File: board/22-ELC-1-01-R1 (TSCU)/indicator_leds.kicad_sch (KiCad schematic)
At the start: 8 parts

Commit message: More work
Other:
- moved on the sheet: D?, R?, U?A
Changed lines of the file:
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@@
   (junction (at 83.82 85.09) (diameter 0) (color 0 0 0 0)
   )
-  (junction (at 85.09 120.65) (diameter 0) (color 0 0 0 0)
-  )
-  (wire (pts (xy 60.96 132.08) (xy 60.96 123.19))
-    (stroke (width 0) (type default) (color 0 0 0 0))
-  )
-  (wire (pts (xy 111.76 120.65) (xy 115.57 120.65))
-    (stroke (width 0) (type default) (color 0 0 0 0))
-  )
-  (wire (pts (xy 85.09 120.65) (xy 85.09 132.08))
+  (junction (at 83.82 120.65) (diameter 0) (color 0 0 0 0)
+  )
+  (wire (pts (xy 59.69 132.08) (xy 59.69 123.19))
+    (stroke (width 0) (type default) (color 0 0 0 0))
+  )
+  (wire (pts (xy 110.49 120.65) (xy 114.3 120.65))
+    (stroke (width 0) (type default) (color 0 0 0 0))
+  )
+  (wire (pts (xy 83.82 120.65) (xy 83.82 132.08))
     (stroke (width 0) (type default) (color 0 0 0 0))
   )
@@
     (stroke (width 0) (type default) (color 0 0 0 0))
   )
-  (wire (pts (xy 90.17 120.65) (xy 85.09 120.65))
-    (stroke (width 0) (type default) (color 0 0 0 0))
-  )
-  (wire (pts (xy 80.01 120.65) (xy 85.09 120.65))
+  (wire (pts (xy 88.9 120.65) (xy 83.82 120.65))
+    (stroke (width 0) (type default) (color 0 0 0 0))
+  )
+  (wire (pts (xy 78.74 120.65) (xy 83.82 120.65))
     (stroke (width 0) (type default) (color 0 0 0 0))
   )
@@
     (stroke (width 0) (type default) (color 0 0 0 0))
   )
-  (wire (pts (xy 115.57 120.65) (xy 115.57 123.19))
+  (wire (pts (xy 114.3 120.65) (xy 114.3 123.19))
     (stroke (width 0) (type default) (color 0 0 0 0))
   )
@@
     (stroke (width 0) (type default) (color 0 0 0 0))
   )
-  (wire (pts (xy 85.09 132.08) (xy 60.96 132.08))
+  (wire (pts (xy 83.82 132.08) (xy 59.69 132.08))
     (stroke (width 0) (type default) (color 0 0 0 0))
   )
@@
     (stroke (width 0) (type default) (color 0 0 0 0))
   )
-  (wire (pts (xy 97.79 120.65) (xy 104.14 120.65))
-    (stroke (width 0) (type default) (color 0 0 0 0))
-  )
-  (wire (pts (xy 46.99 118.11) (xy 64.77 118.11))
-    (stroke (width 0) (type default) (color 0 0 0 0))
-  )
-  (wire (pts (xy 60.96 123.19) (xy 64.77 123.19))
+  (wire (pts (xy 96.52 120.65) (xy 102.87 120.65))
+    (stroke (width 0) (type default) (color 0 0 0 0))
+  )
+  (wire (pts (xy 46.99 118.11) (xy 63.5 118.11))
+    (stroke (width 0) (type default) (color 0 0 0 0))
+  )
+  (wire (pts (xy 59.69 123.19) (xy 63.5 123.19))
     (stroke (width 0) (type default) (color 0 0 0 0))
   )
@@
     (pin "8")
   )
-  (symbol (lib_id "power:GND") (at 115.57 123.19 0) (unit 1)
-    (in_bom yes) (on_board yes) (fields_autoplaced)
-    (property "Reference" "#PWR?" (id 0) (at 115.57 129.54 0)
-      (effects (font (size 1.27 1.27)) hide)
-    )
-    (property "Value" "GND" (id 1) (at 115.57 128.27 0))
-    (property "Footprint" "" (id 2) (at 115.57 123.19 0)
-      (effects (font (size 1.27 1.27)) hide)
-    )
-    (property "Datasheet" "" (id 3) (at 115.57 123.19 0)
-      (effects (font (size 1.27 1.27)) hide)
-    )
-    (pin "1")
-  )
-  (symbol (lib_id "Amplifier_Operational:LM358") (at 72.39 120.65 0) (unit 1)
-    (in_bom yes) (on_board yes) (fields_autoplaced)
-    (property "Reference" "U?" (id 0) (at 72.39 110.49 0))
-    (property "Value" "LM358" (id 1) (at 72.39 113.03 0))
-    (property "Footprint" "" (id 2) (at 72.39 120.65 0)
-      (effects (font (size 1.27 1.27)) hide)
-    )
-    (property "Datasheet" "http://www.ti.com/lit/ds/symlink/lm2904-n.pdf" (id 3) (at 72.39 120.65 0)
+  (symbol (lib_id "power:GND") (at 114.3 123.19 0) (unit 1)
+    (in_bom yes) (on_board yes) (fields_autoplaced)
+    (property "Reference" "#PWR?" (id 0) (at 114.3 129.54 0)
+      (effects (font (size 1.27 1.27)) hide)
+    )
+    (property "Value" "GND" (id 1) (at 114.3 128.27 0))
+    (property "Footprint" "" (id 2) (at 114.3 123.19 0)
+      (effects (font (size 1.27 1.27)) hide)
+    )
+    (property "Datasheet" "" (id 3) (at 114.3 123.19 0)
+      (effects (font (size 1.27 1.27)) hide)
+    )
+    (pin "1")
+  )
+  (symbol (lib_id "Amplifier_Operational:LM358") (at 71.12 120.65 0) (unit 1)
+    (in_bom yes) (on_board yes) (fields_autoplaced)
+    (property "Reference" "U?" (id 0) (at 71.12 110.49 0))
+    (property "Value" "LM358" (id 1) (at 71.12 113.03 0))
+    (property "Footprint" "" (id 2) (at 71.12 120.65 0)
+      (effects (font (size 1.27 1.27)) hide)
+    )
+    (property "Datasheet" "http://www.ti.com/lit/ds/symlink/lm2904-n.pdf" (id 3) (at 71.12 120.65 0)
       (effects (font (size 1.27 1.27)) hide)
     )
@@
     (pin "8")
   )
-  (symbol (lib_id "Device:R") (at 93.98 120.65 90) (unit 1)
-    (in_bom yes) (on_board yes) (fields_autoplaced)
-    (property "Reference" "R?" (id 0) (at 93.98 114.3 90))
-    (property "Value" "220" (id 1) (at 93.98 116.84 90))
-    (property "Footprint" "" (id 2) (at 93.98 122.428 90)
-      (effects (font (size 1.27 1.27)) hide)
-    )
-    (property "Datasheet" "~" (id 3) (at 93.98 120.65 0)
-      (effects (font (size 1.27 1.27)) hide)
-    )
-    (pin "1")
-    (pin "2")
-  )
-  (symbol (lib_id "Device:LED") (at 107.95 120.65 180) (unit 1)
-    (in_bom yes) (on_board yes) (fields_autoplaced)
-    (property "Reference" "D?" (id 0) (at 109.5375 113.03 0))
-    (property "Value" "IMS_FAULT_LED" (id 1) (at 109.5375 115.57 0))
-    (property "Footprint" "" (id 2) (at 107.95 120.65 0)
-      (effects (font (size 1.27 1.27)) hide)
-    )
-    (property "Datasheet" "~" (id 3) (at 107.95 120.65 0)
-      (effects (font (size 1.27 1.27)) hide)
-    )
+  (symbol (lib_id "Device:R") (at 92.71 120.65 90) (unit 1)
+    (in_bom yes) (on_board yes) (fields_autoplaced)
+    (property "Reference" "R?" (id 0) (at 92.71 114.3 90))
+    (property "Value" "220" (id 1) (at 92.71 116.84 90))
+    (property "Footprint" "" (id 2) (at 92.71 122.428 90)
+      (effects (font (size 1.27 1.27)) hide)
+    )
+    (property "Datasheet" "~" (id 3) (at 92.71 120.65 0)
+      (effects (font (size 1.27 1.27)) hide)
+    )
+    (pin "1")
+    (pin "2")
+  )
+  (symbol (lib_id "Device:LED") (at 106.68 120.65 180) (unit 1)
+    (in_bom yes) (on_board yes) (fields_autoplaced)
+    (property "Reference" "D?" (id 0) (at 108.2675 113.03 0))
+    (property "Value" "IMS_FAULT_LED" (id 1) (at 108.2675 115.57 0))
+    (property "Footprint" "" (id 2) (at 106.68 120.65 0)
+      (effects (font (size 1.27 1.27)) hide)
+    )
+    (property "Datasheet" "~" (id 3) (at 106.68 120.65 0)
+      (effects (font (size 1.27 1.27)) hide)
+    )

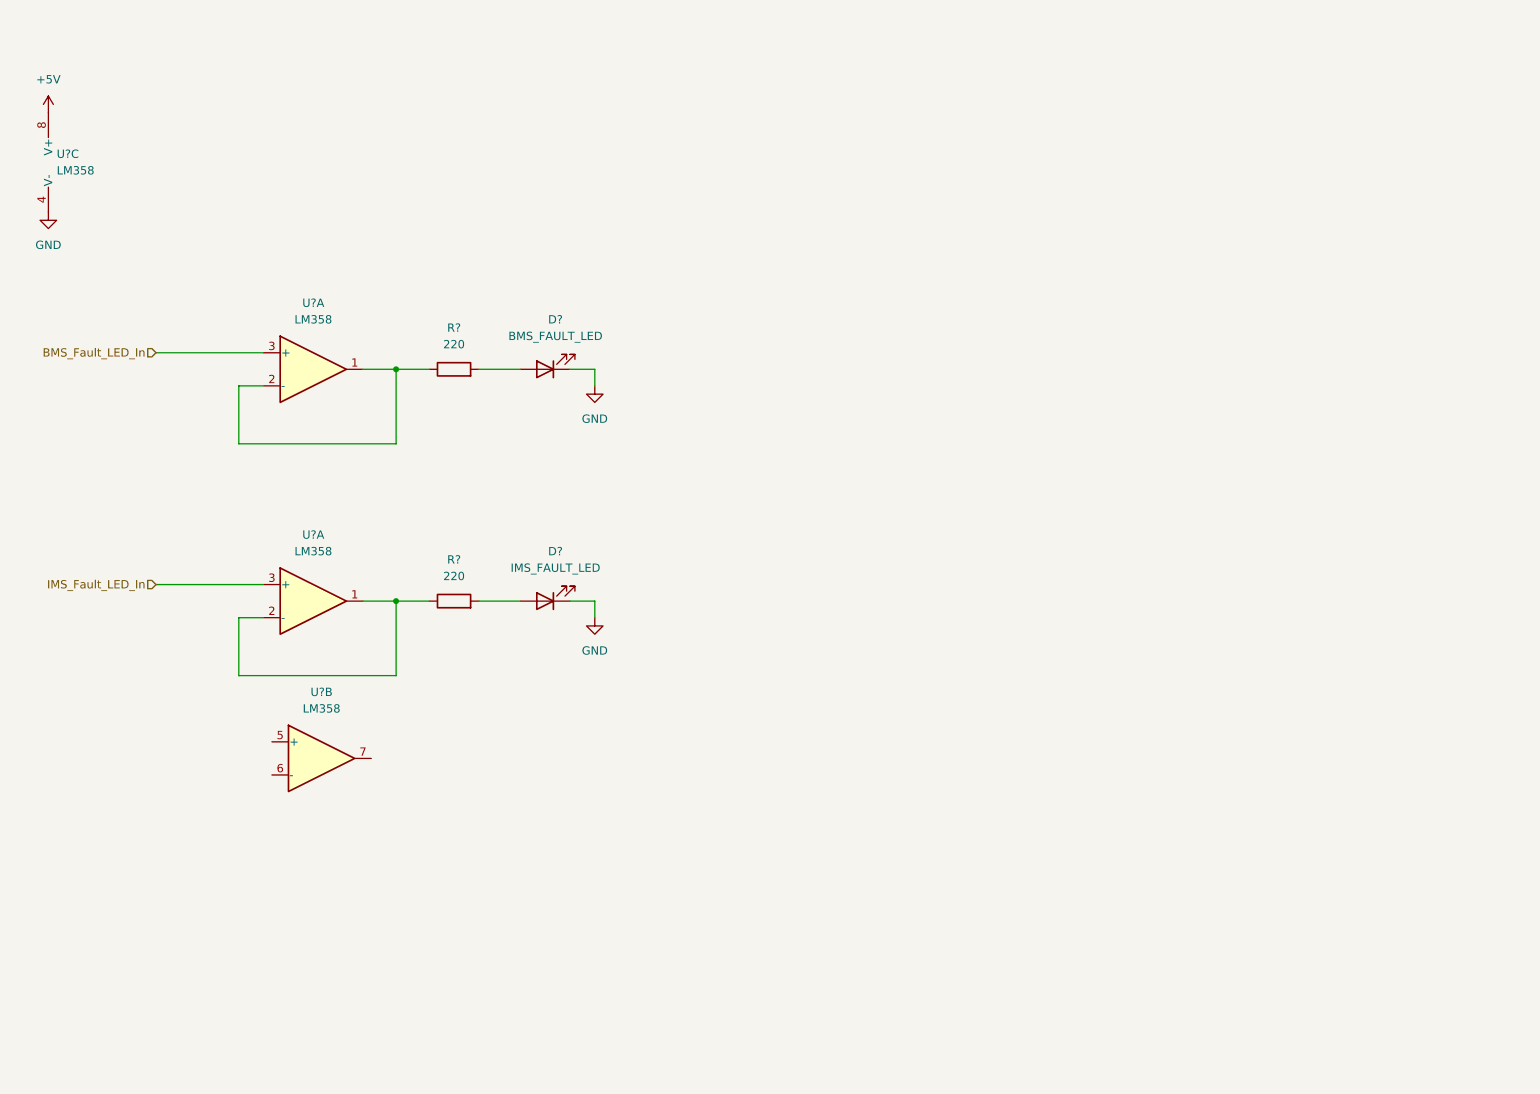
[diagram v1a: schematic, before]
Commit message: More LEDs and test points
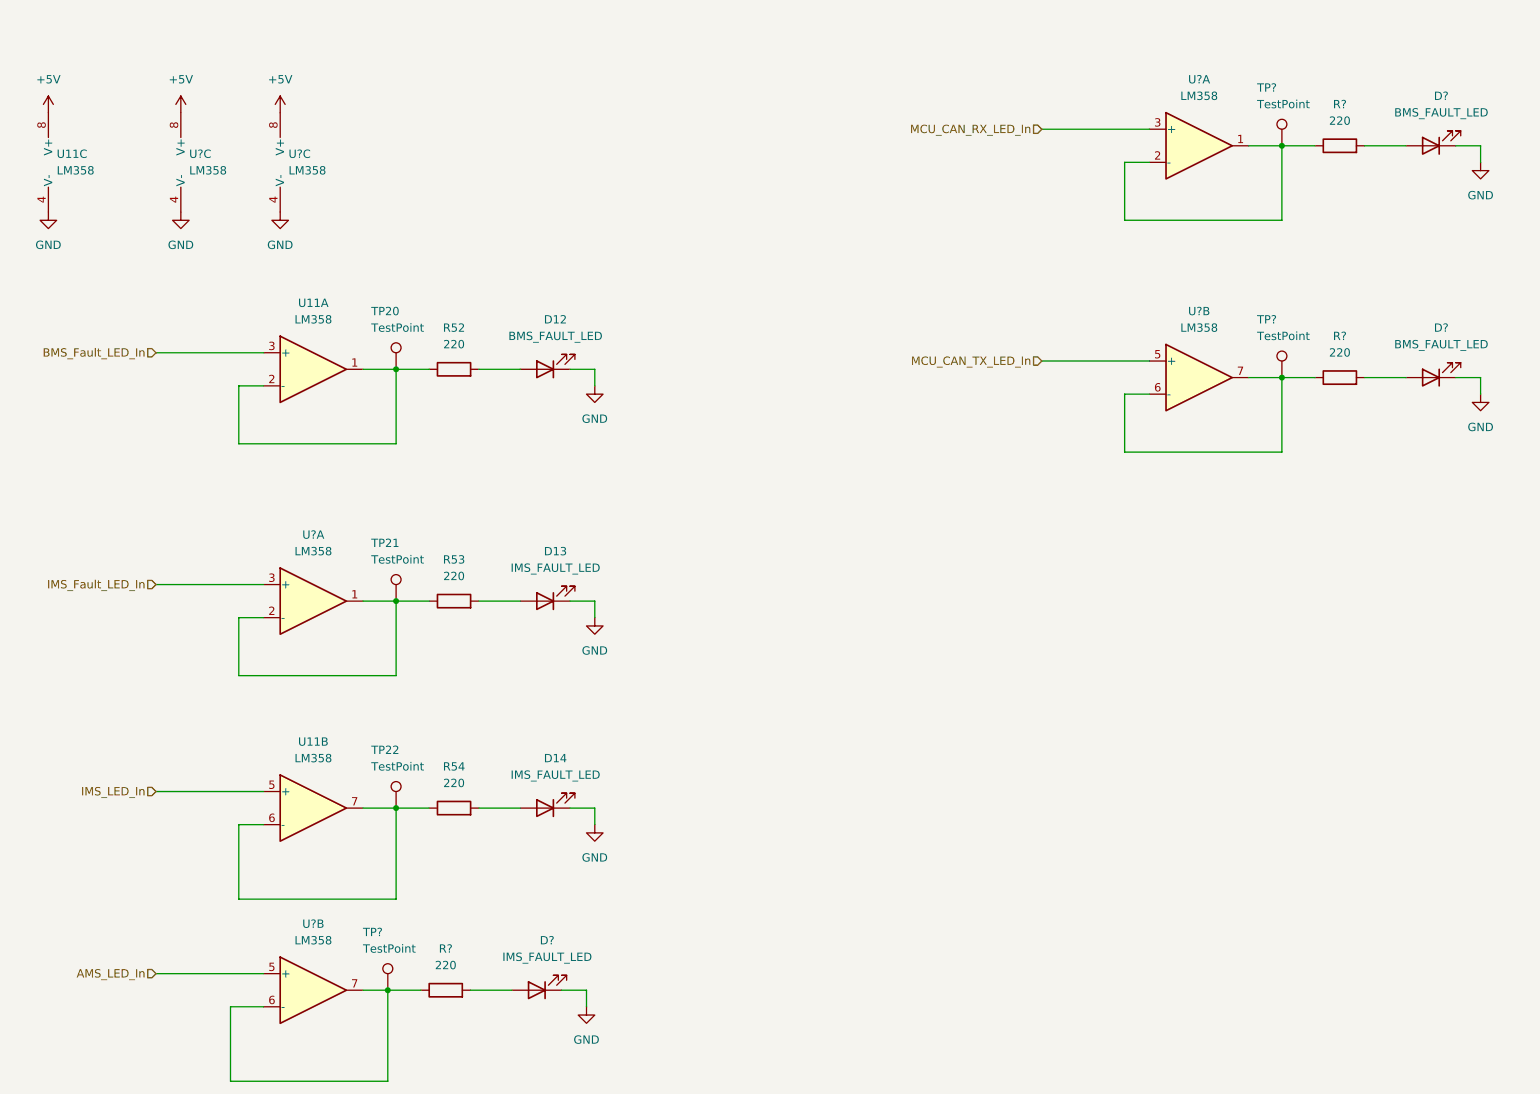
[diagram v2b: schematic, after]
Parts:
- removed U?: LM358, symbol Amplifier_Operational:LM358
- added D14, D?: IMS_FAULT_LED, symbol Device:LED
- added D? (x2): BMS_FAULT_LED, symbol Device:LED
- added R54, R? (x3): 220, symbol Device:R
- added TP20, TP21, TP22, TP? (x3): TestPoint, symbol Connector:TestPoint
- added U? (x6): LM358, symbol Amplifier_Operational:LM358
- gave numbers to parts that had none: 5
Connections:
- net +5V: now also U?.8 (V+), U?.8 (V+)
- net GND: now also D14.1 (K), D?.1 (K), D?.1 (K), D?.1 (K), U?.4 (V-), U?.4 (V-)
- net IMS_Fault_LED_In: now also U?.3 (+)
- net IMS_LED_In: now reaches U11.5 (+)
- net at U11.6 (-): now also U11.7, R54.1, TP22.1
- net at R53.1: now also TP21.1, U?.1, U?.2 (-)
- net at R52.1, U11.1, U11.2 (-): now also TP20.1
- new net: R?.1, TP?.1, U?.6 (-), U?.7 (x2)
- new net: D14.2 (A), R54.2
- new net: R?.1, TP?.1, U?.1, U?.2 (-)
- new net: D?.2 (A), R?.2 (x3)
- new net AMS_LED_In: U?.5 (+)
- new net MCU_CAN_RX_LED_In: U?.3 (+)
- new net MCU_CAN_TX_LED_In: U?.5 (+)
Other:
- moved on the sheet: U11B

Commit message: More LEDs and TPs
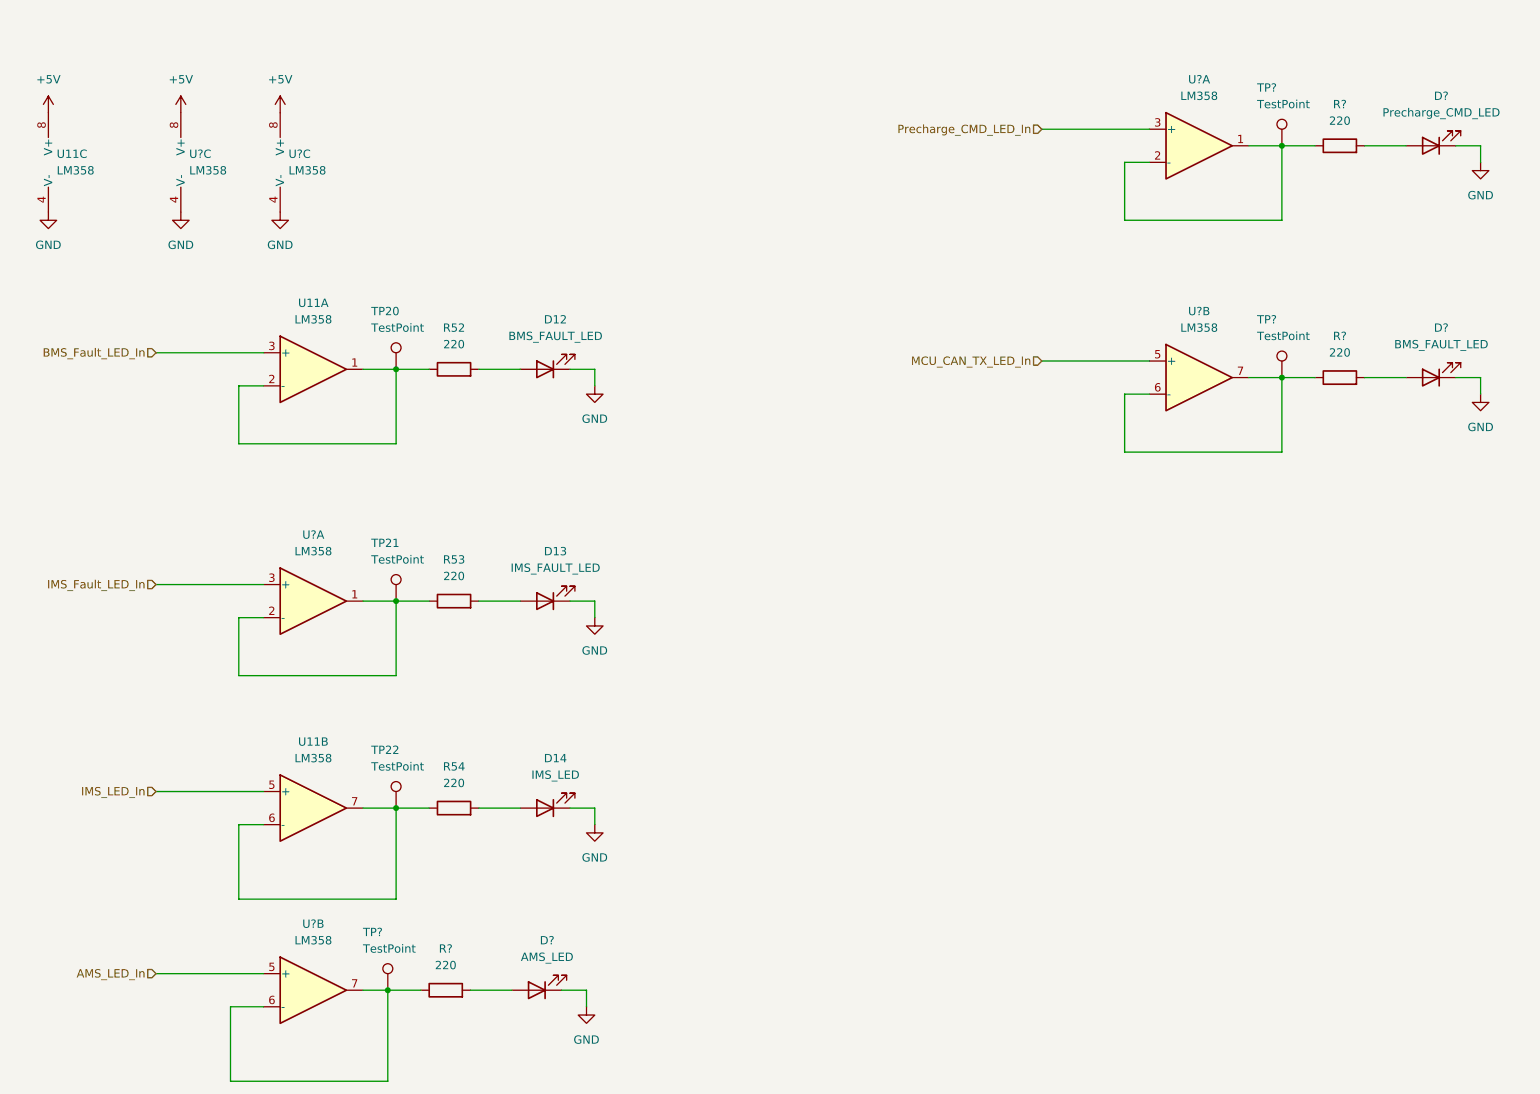
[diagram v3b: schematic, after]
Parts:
- D14: value IMS_FAULT_LED -> IMS_LED
- D?: value BMS_FAULT_LED -> Precharge_CMD_LED
- D?: value IMS_FAULT_LED -> AMS_LED
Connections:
- net MCU_CAN_RX_LED_In renamed Precharge_CMD_LED_In
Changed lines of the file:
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@@
     (effects (font (size 1.27 1.27)) (justify right))
   )
-  (hierarchical_label "MCU_CAN_RX_LED_In" (shape input) (at 182.88 48.26 180)
+  (hierarchical_label "Precharge_CMD_LED_In" (shape input) (at 182.88 48.26 180)
     (effects (font (size 1.27 1.27)) (justify right))
   )
@@
     (in_bom yes) (on_board yes) (fields_autoplaced)
     (property "Reference" "D?" (id 0) (at 244.1575 43.18 0))
-    (property "Value" "BMS_FAULT_LED" (id 1) (at 244.1575 45.72 0))
+    (property "Value" "Precharge_CMD_LED" (id 1) (at 244.1575 45.72 0))
     (property "Footprint" "" (id 2) (at 242.57 50.8 0)
       (effects (font (size 1.27 1.27)) hide)
@@
     (in_bom yes) (on_board yes) (fields_autoplaced)
     (property "Reference" "D14" (id 0) (at 108.2675 144.78 0))
-    (property "Value" "IMS_FAULT_LED" (id 1) (at 108.2675 147.32 0))
+    (property "Value" "IMS_LED" (id 1) (at 108.2675 147.32 0))
     (property "Footprint" "" (id 2) (at 106.68 152.4 0)
       (effects (font (size 1.27 1.27)) hide)
@@
     (in_bom yes) (on_board yes) (fields_autoplaced)
     (property "Reference" "D?" (id 0) (at 106.9975 172.72 0))
-    (property "Value" "IMS_FAULT_LED" (id 1) (at 106.9975 175.26 0))
+    (property "Value" "AMS_LED" (id 1) (at 106.9975 175.26 0))
     (property "Footprint" "" (id 2) (at 105.41 180.34 0)
       (effects (font (size 1.27 1.27)) hide)

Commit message: Ready for review
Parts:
- D17: renamed from D?; value BMS_FAULT_LED -> Final_Close_Out_LED
- gave numbers to parts that had none: 10
- renumbered D12 to D13, D13 to D14, D14 to D15, R52 to R53, R53 to R54, R54 to R55, TP20 to TP21, TP21 to TP22, TP22 to TP23, U11 to U12
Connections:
- net MCU_CAN_TX_LED_In renamed Final_Precharge_Close_Out_LED_In
